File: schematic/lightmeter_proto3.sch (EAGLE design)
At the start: 75 parts, among them J1 AVR_SPI_PRG_6NS, Q1 NCHANNELMOSFET, Q10 NCHANNELMOSFET, Q11 NCHANNELMOSFET, Q12 NCHANNELMOSFET, Q16 PCHANNELMOSFET, Q2 PCHANNELMOSFET, Q3 NCHANNELMOSFET, Q4 PCHANNELMOSFET, Q5 NCHANNELMOSFET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

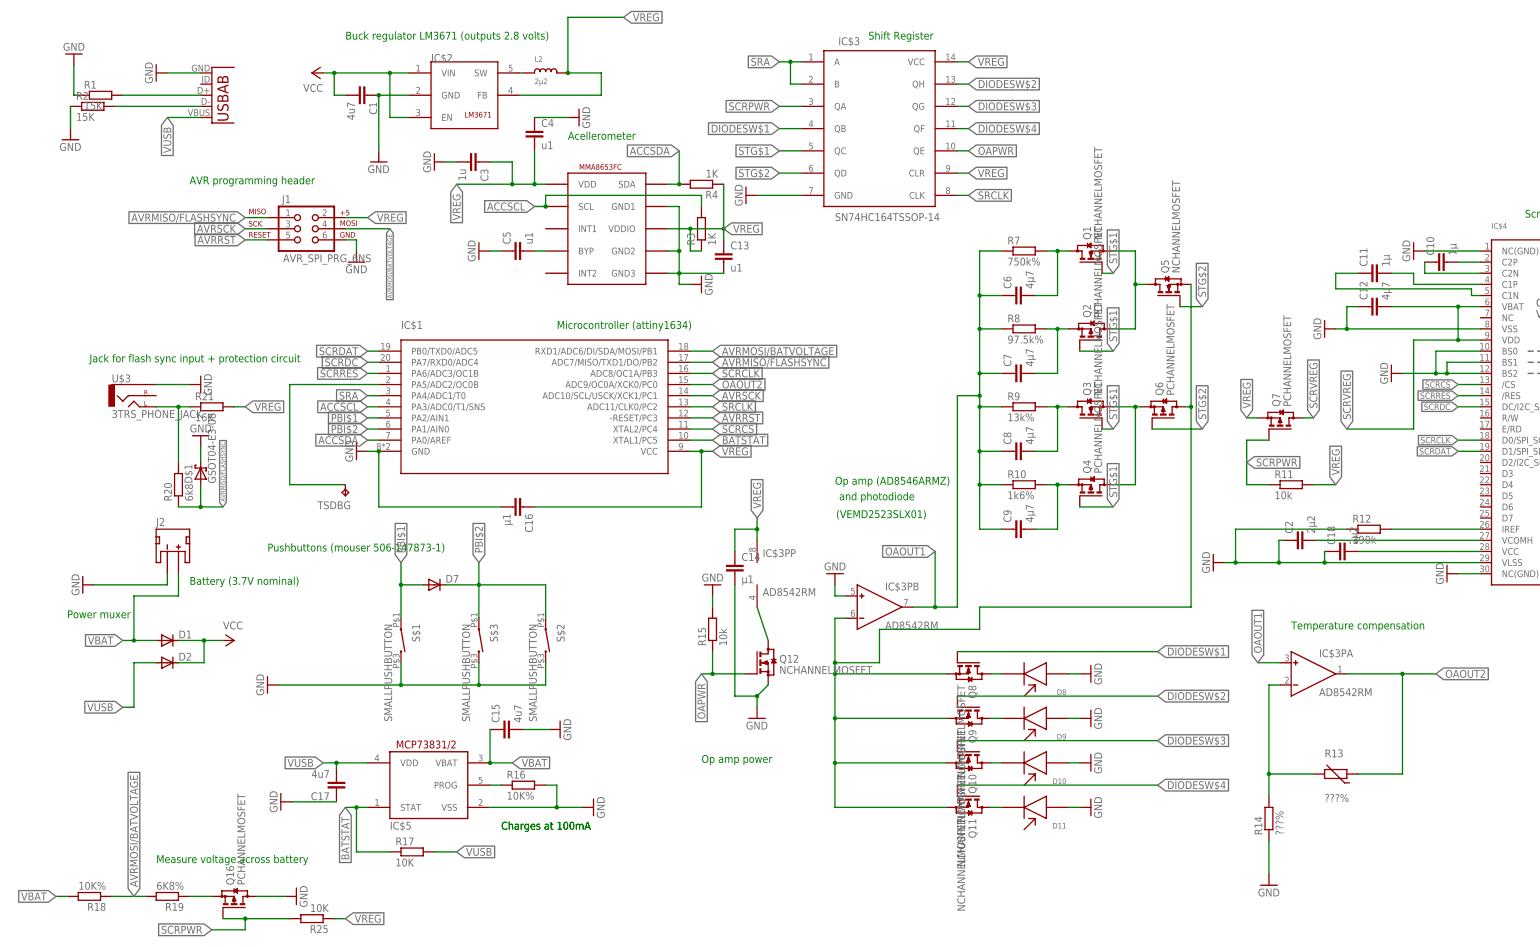
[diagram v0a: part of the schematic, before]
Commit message: Make naming of values systematic in proto boards.
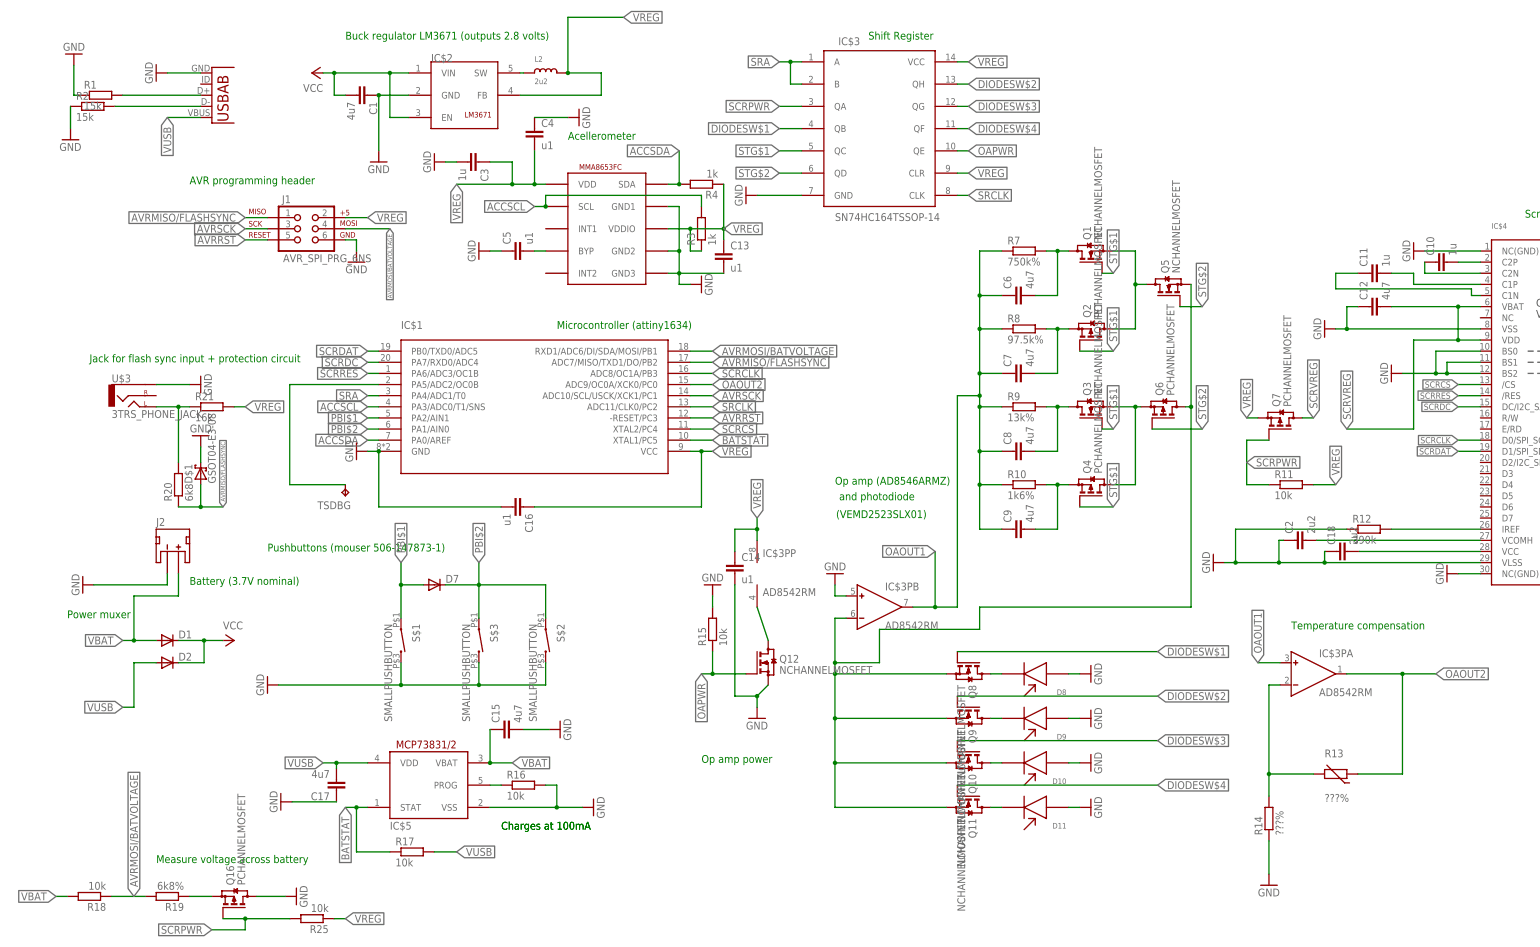
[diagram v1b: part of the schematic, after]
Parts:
- C10, C11: value 1µ -> 1u
- C12, C6, C7, C8, C9: value 4µ7 -> 4u7
- C14, C16: value µ1 -> u1
- C18, C2, L2: value 2µ2 -> 2u2
- R1, R2: value 15K -> 15k
- R16, R18: value 10K% -> 10k
- R17, R25: value 10K -> 10k
- R19: value 6K8% -> 6k8%
- R21: value 16K -> 16k
- R3, R4: value 1K -> 1k
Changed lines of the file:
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@@
 <part name="IC$3P" library="analog-devices" deviceset="AD8542" device="RM" value="AD8542RM"/>
 <part name="GND2" library="supply1" deviceset="GND" device=""/>
-<part name="C14" library="rcl" deviceset="C-EU" device="C0402" value="µ1"/>
+<part name="C14" library="rcl" deviceset="C-EU" device="C0402" value="u1"/>
 <part name="IC$4" library="microbuilder" deviceset="DISP_OLED_UG-2864HSWEG01" device="0.96&quot;"/>
 <part name="R9" library="resistor" deviceset="R-EU_" device="R0402" value="13k%"/>
@@
 <part name="GND11" library="supply1" deviceset="GND" device=""/>
 <part name="GND12" library="supply1" deviceset="GND" device=""/>
-<part name="C16" library="rcl" deviceset="C-EU" device="C0402" value="µ1"/>
+<part name="C16" library="rcl" deviceset="C-EU" device="C0402" value="u1"/>
 <part name="GND13" library="supply1" deviceset="GND" device=""/>
 <part name="GND15" library="supply1" deviceset="GND" device=""/>
@@
 <part name="D7" library="diode2" deviceset="DIODE-" device="SOD323-W"/>
 <part name="R8" library="resistor" deviceset="R-EU_" device="R0402" value="97.5k%"/>
-<part name="C9" library="rcl" deviceset="C-EU" device="C0402" value="4µ7"/>
-<part name="C8" library="rcl" deviceset="C-EU" device="C0402" value="4µ7"/>
-<part name="C7" library="rcl" deviceset="C-EU" device="C0402" value="4µ7"/>
+<part name="C9" library="rcl" deviceset="C-EU" device="C0402" value="4u7"/>
+<part name="C8" library="rcl" deviceset="C-EU" device="C0402" value="4u7"/>
+<part name="C7" library="rcl" deviceset="C-EU" device="C0402" value="4u7"/>
 <part name="GND5" library="supply1" deviceset="GND" device=""/>
 <part name="GND18" library="supply1" deviceset="GND" device=""/>
 <part name="GND19" library="supply1" deviceset="GND" device=""/>
 <part name="GND20" library="supply1" deviceset="GND" device=""/>
-<part name="C6" library="rcl" deviceset="C-EU" device="C0402" value="4µ7"/>
+<part name="C6" library="rcl" deviceset="C-EU" device="C0402" value="4u7"/>
 <part name="R7" library="resistor" deviceset="R-EU_" device="R0402" value="750k%"/>
 <part name="D8" library="lightmeter" deviceset="VEMD2523SLX01" device=""/>
@@
 <part name="D11" library="lightmeter" deviceset="VEMD2523SLX01" device=""/>
 <part name="R12" library="resistor" deviceset="R-EU_" device="R0402" value="390k"/>
-<part name="C10" library="rcl" deviceset="C-EU" device="C0402" value="1µ"/>
-<part name="C11" library="rcl" deviceset="C-EU" device="C0402" value="1µ"/>
+<part name="C10" library="rcl" deviceset="C-EU" device="C0402" value="1u"/>
+<part name="C11" library="rcl" deviceset="C-EU" device="C0402" value="1u"/>
 <part name="GND17" library="supply1" deviceset="GND" device=""/>
 <part name="GND21" library="supply1" deviceset="GND" device=""/>
 <part name="GND22" library="supply1" deviceset="GND" device=""/>
-<part name="C12" library="rcl" deviceset="C-EU" device="C0402" value="4µ7"/>
+<part name="C12" library="rcl" deviceset="C-EU" device="C0402" value="4u7"/>
 <part name="GND3" library="supply1" deviceset="GND" device=""/>
 <part name="J1" library="SparkFun-Connectors" deviceset="AVR_SPI_PRG_6" device="NS"/>
 <part name="GND14" library="supply1" deviceset="GND" device=""/>
 <part name="IC$1" library="attiny1634_corrected" deviceset="ATTINY1634" device="MLF20"/>
-<part name="L2" library="microbuilder" deviceset="INDUCTOR" device="_0603" value="2µ2"/>
+<part name="L2" library="microbuilder" deviceset="INDUCTOR" device="_0603" value="2u2"/>
 <part name="GND23" library="supply1" deviceset="GND" device=""/>
 <part name="Q8" library="lightmeter" deviceset="NCHANNELMOSFET" device=""/>
@@
 <part name="IC$5" library="adafruit" deviceset="MCP73831" device="/OT"/>
 <part name="GND6" library="supply1" deviceset="GND" device=""/>
-<part name="R17" library="resistor" deviceset="R-EU_" device="R0402" value="10K"/>
-<part name="R16" library="resistor" deviceset="R-EU_" device="R0402" value="10K%"/>
+<part name="R17" library="resistor" deviceset="R-EU_" device="R0402" value="10k"/>
+<part name="R16" library="resistor" deviceset="R-EU_" device="R0402" value="10k"/>
 <part name="J2" library="SparkFun-Connectors" deviceset="JST_2MM_MALE" device=""/>
 <part name="GND26" library="supply1" deviceset="GND" device=""/>
@@
 <part name="U$3" library="lightmeter" deviceset="3TRS_PHONE_JACK" device=""/>
 <part name="GND10" library="supply1" deviceset="GND" device=""/>
-<part name="R21" library="resistor" deviceset="R-EU_" device="R0402" value="16K"/>
+<part name="R21" library="resistor" deviceset="R-EU_" device="R0402" value="16k"/>
 <part name="R20" library="resistor" deviceset="R-EU_" device="R0402" value="6k8"/>
 <part name="GND30" library="supply1" deviceset="GND" device=""/>
@@
 <part name="S$3" library="lightmeter" deviceset="SMALLPUSHBUTTON" device=""/>
 <part name="S$2" library="lightmeter" deviceset="SMALLPUSHBUTTON" device=""/>
-<part name="R18" library="resistor" deviceset="R-EU_" device="R0402" value="10K%"/>
-<part name="R19" library="resistor" deviceset="R-EU_" device="R0402" value="6K8%"/>
+<part name="R18" library="resistor" deviceset="R-EU_" device="R0402" value="10k"/>
+<part name="R19" library="resistor" deviceset="R-EU_" device="R0402" value="6k8%"/>
 <part name="GND32" library="supply1" deviceset="GND" device=""/>
 <part name="GND31" library="supply1" deviceset="GND" device=""/>
-<part name="R1" library="resistor" deviceset="R-EU_" device="R0402" value="15K"/>
-<part name="R2" library="resistor" deviceset="R-EU_" device="R0402" value="15K"/>
+<part name="R1" library="resistor" deviceset="R-EU_" device="R0402" value="15k"/>
+<part name="R2" library="resistor" deviceset="R-EU_" device="R0402" value="15k"/>
 <part name="GND9" library="supply1" deviceset="GND" device=""/>
 <part name="GND33" library="supply1" deviceset="GND" device=""/>
 <part name="C17" library="rcl" deviceset="C-EU" device="C0402" value="4u7"/>
 <part name="GND34" library="supply1" deviceset="GND" device=""/>
-<part name="R25" library="resistor" deviceset="R-EU_" device="R0402" value="10K"/>
+<part name="R25" library="resistor" deviceset="R-EU_" device="R0402" value="10k"/>
 <part name="Q16" library="lightmeter" deviceset="PCHANNELMOSFET" device=""/>
 <part name="D$1" library="lightmeter" deviceset="GSOT04-E3-08" device=""/>
-<part name="C18" library="rcl" deviceset="C-EU" device="C0402" value="2µ2"/>
+<part name="C18" library="rcl" deviceset="C-EU" device="C0402" value="2u2"/>
 <part name="D1" library="diode2" deviceset="DIODE-" device="SOD323-W"/>
 <part name="D2" library="diode2" deviceset="DIODE-" device="SOD323-W"/>
-<part name="C2" library="rcl" deviceset="C-EU" device="C0402" value="2µ2"/>
+<part name="C2" library="rcl" deviceset="C-EU" device="C0402" value="2u2"/>
 <part name="IC$6" library="lightmeter" deviceset="MMA8653" device=""/>
 <part name="C3" library="rcl" deviceset="C-EU" device="C0402" value="1u"/>
@@
 <part name="C5" library="rcl" deviceset="C-EU" device="C0402" value="u1"/>
 <part name="GND16" library="supply1" deviceset="GND" device=""/>
-<part name="R3" library="resistor" deviceset="R-EU_" device="R0402" value="1K"/>
-<part name="R4" library="resistor" deviceset="R-EU_" device="R0402" value="1K"/>
+<part name="R3" library="resistor" deviceset="R-EU_" device="R0402" value="1k"/>
+<part name="R4" library="resistor" deviceset="R-EU_" device="R0402" value="1k"/>
 <part name="C13" library="rcl" deviceset="C-EU" device="C0402" value="u1"/>
 <part name="U1" library="lightmeter" deviceset="USB-AB" device=""/>
